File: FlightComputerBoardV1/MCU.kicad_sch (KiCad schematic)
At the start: 22 parts, among them U20 STM32H723ZGTx

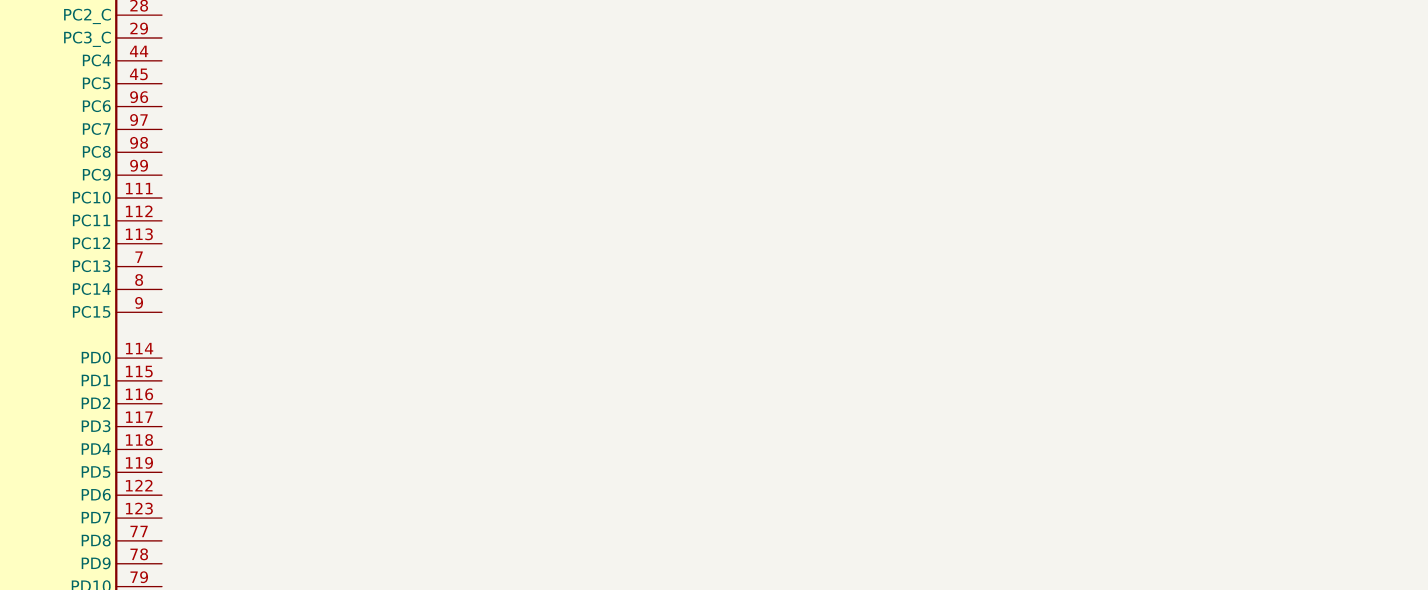
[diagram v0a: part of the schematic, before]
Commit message: Added external clk for mcu sheet
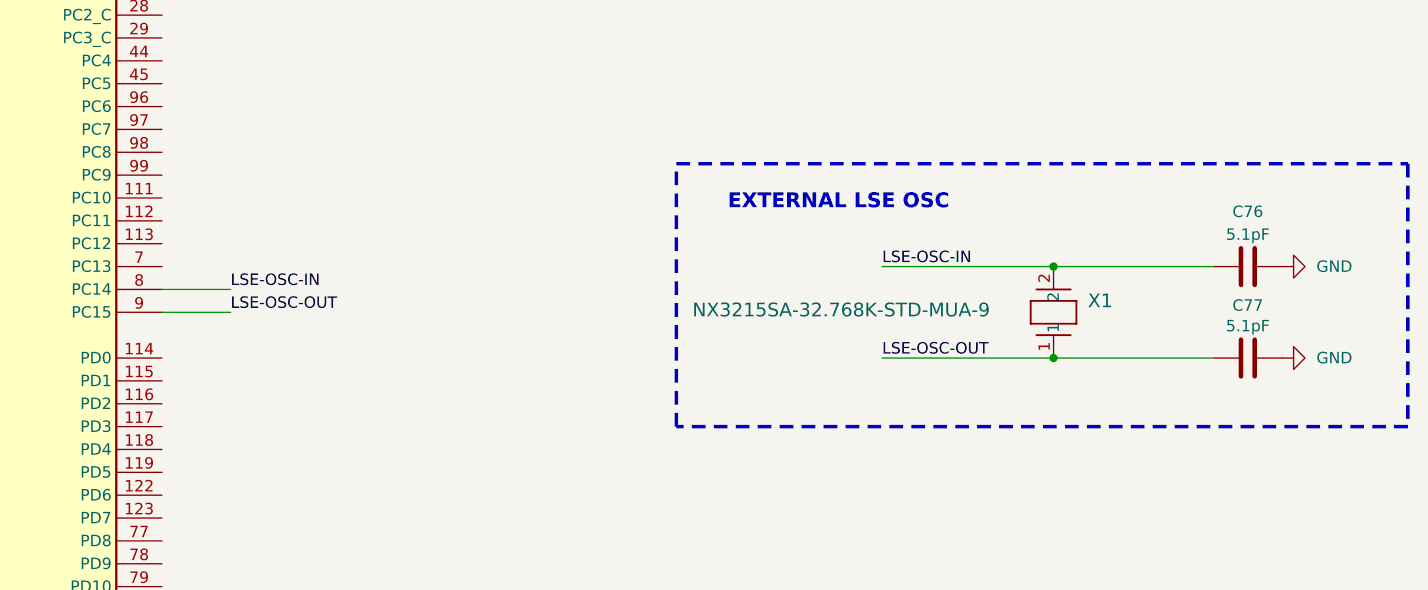
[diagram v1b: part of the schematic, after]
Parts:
- added C76, C77: 5.1pF, XTAL_NX3215SA_NDK, symbol Device:C
- added X1: NX3215SA-32.768K-STD-MUA-9, XTAL_NX3215SA_NDK, symbol LSE-OSC:NX3215SA-32.768K-STD-MUA-9
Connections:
- net GND: now also C76.2, C77.1
- net LSE-OSC-IN: now reaches U20.8 (PC14)
- net LSE-OSC-IN: now also C76.1, X1.2
- net LSE-OSC-OUT: now reaches U20.9 (PC15)
- net LSE-OSC-OUT: now also C77.2, X1.1
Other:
- note added: "EXTERNAL LSE OSC"

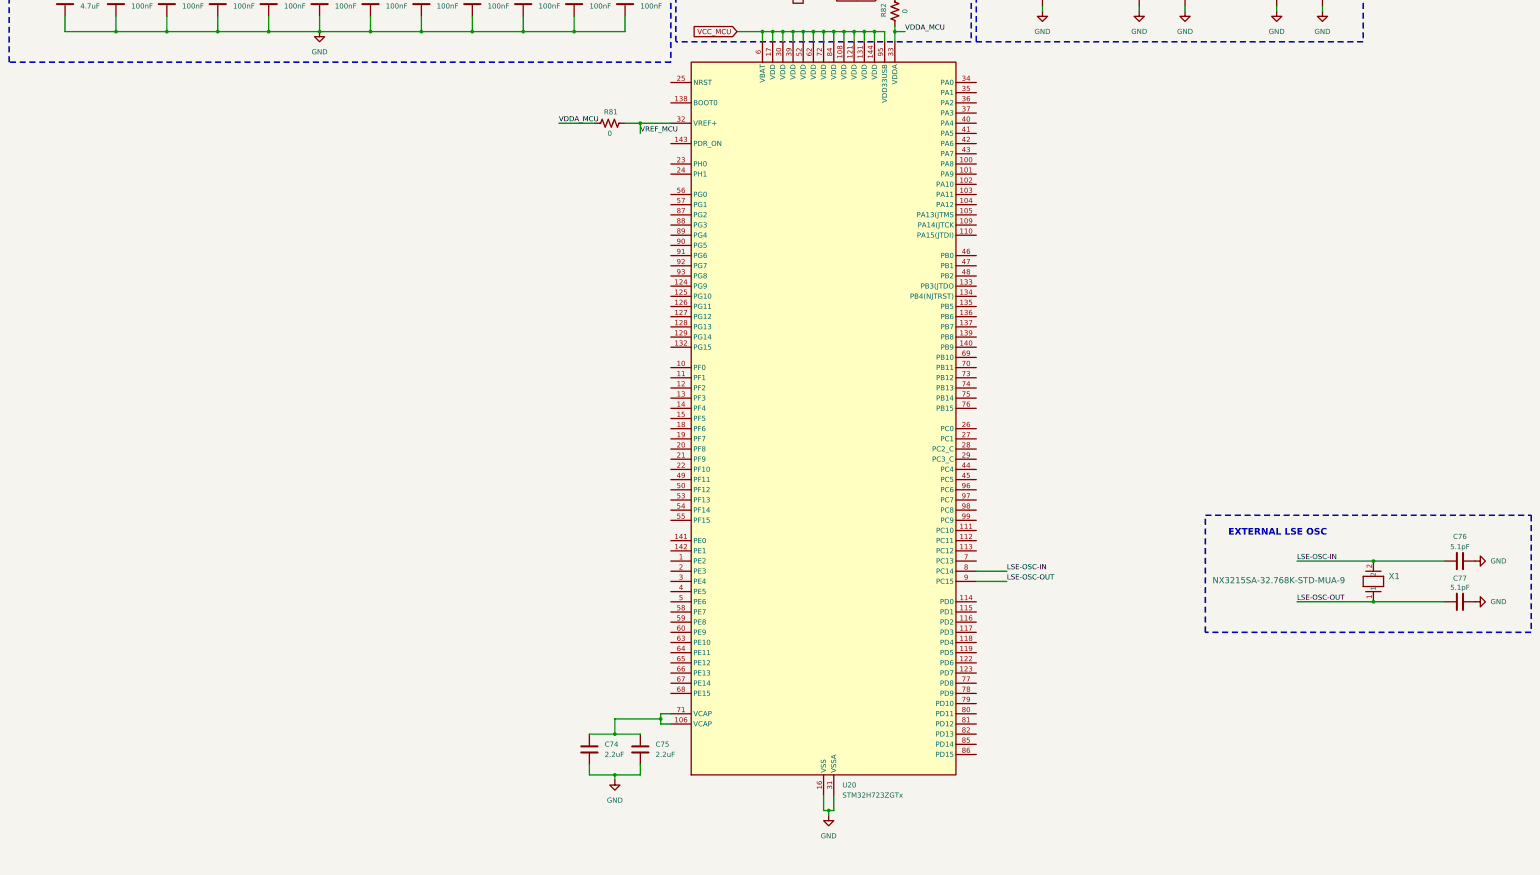
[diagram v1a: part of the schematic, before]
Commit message: Addition to MCU sheet and peripheral connection complete
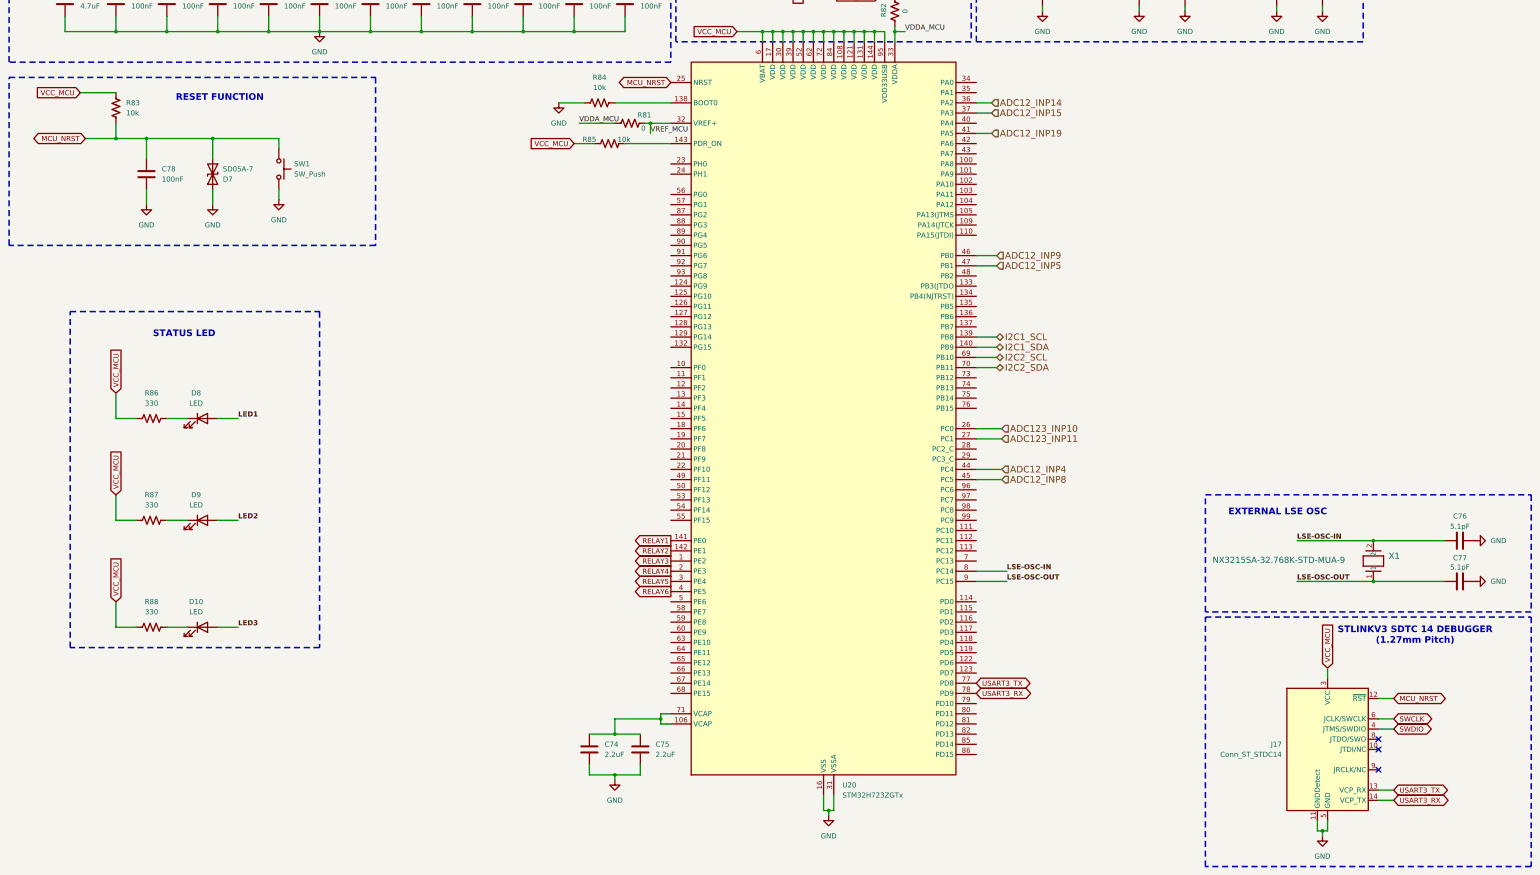
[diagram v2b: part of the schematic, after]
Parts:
- added C78: 100nF, symbol Device:C
- added D10, D8, D9: LED, symbol Device:LED
- added D7: SD05A-7, Diode_SMD:D_SOD-323_HandSoldering, symbol Diode:SD05C-01F
- added J17: Conn_ST_STDC14, Connector_PinHeader_1.27mm:PinHeader_2x07_P1.27mm_Vertical, symbol Connector:Conn_ST_STDC14
- added R83, R84, R85: 10k, Resistor_THT:R_Array_SIP4, symbol Device:R_US
- added R86, R87, R88: 330, Resistor_THT:R_Array_SIP4, symbol Device:R_US
- added SW1: SW_Push, Button_Switch_THT:SW_PUSH_6mm_H4.3mm, symbol Switch:SW_Push
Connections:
- net +3V3: now also J17.3 (VCC), R83.1, R85.1, R86.1, R87.1, R88.1
- net GND: now also C78.2, D7.2 (A2), J17.11 (GNDDetect), J17.5 (GND), J17.7 (GND), R84.1, SW1.2
- net RELAY3: now reaches U20.1 (PE2)
- net at U20.138 (BOOT0): now also R84.2
- net I2C1_SCL: now reaches U20.139 (PB8)
- net I2C1_SDA: now reaches U20.140 (PB9)
- net RELAY1: now reaches U20.141 (PE0)
- net RELAY2: now reaches U20.142 (PE1)
- net at U20.143 (PDR_ON): now also R85.2
- net RELAY4: now reaches U20.2 (PE3)
- net MCU_NRST: now reaches U20.25 (NRST)
- net MCU_NRST: now also C78.1, D7.1 (A1), J17.12 (~{RST}), R83.2, SW1.1
- net ADC123_INP10: now reaches U20.26 (PC0)
- net ADC123_INP11: now reaches U20.27 (PC1)
- net RELAY5: now reaches U20.3 (PE4)
- net ADC12_INP14: now reaches U20.36 (PA2)
- net ADC12_INP15: now reaches U20.37 (PA3)
- net RELAY6: now reaches U20.4 (PE5)
- net ADC12_INP19: now reaches U20.41 (PA5)
- net ADC12_INP4: now reaches U20.44 (PC4)
- net ADC12_INP8: now reaches U20.45 (PC5)
- net ADC12_INP9: now reaches U20.46 (PB0)
- net ADC12_INP5: now reaches U20.47 (PB1)
- net I2C2_SCL: now reaches U20.69 (PB10)
- net I2C2_SDA: now reaches U20.70 (PB11)
- net USART3_TX: now reaches U20.77 (PD8)
- net USART3_TX: now also J17.13 (VCP_RX)
- net USART3_RX: now reaches U20.78 (PD9)
- net USART3_RX: now also J17.14 (VCP_TX)
- new net: D9.1 (K), R87.2
- new net: D8.1 (K), R86.2
- new net: D10.1 (K), R88.2
- new net LED1: D8.2 (A)
- new net LED2: D9.2 (A)
- new net LED3: D10.2 (A)
- new net SWCLK: J17.6 (JCLK/SWCLK)
- new net SWDIO: J17.4 (JTMS/SWDIO)
- no-connect marks 0 -> 3
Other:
- note added: "RESET FUNCTION"
- note added: "STATUS LED"
- note added: "STLINKV3 SDTC 14 DEBUGGER (1.27mm Pitch)"
- moved on the sheet: C76, C77, R81, X1

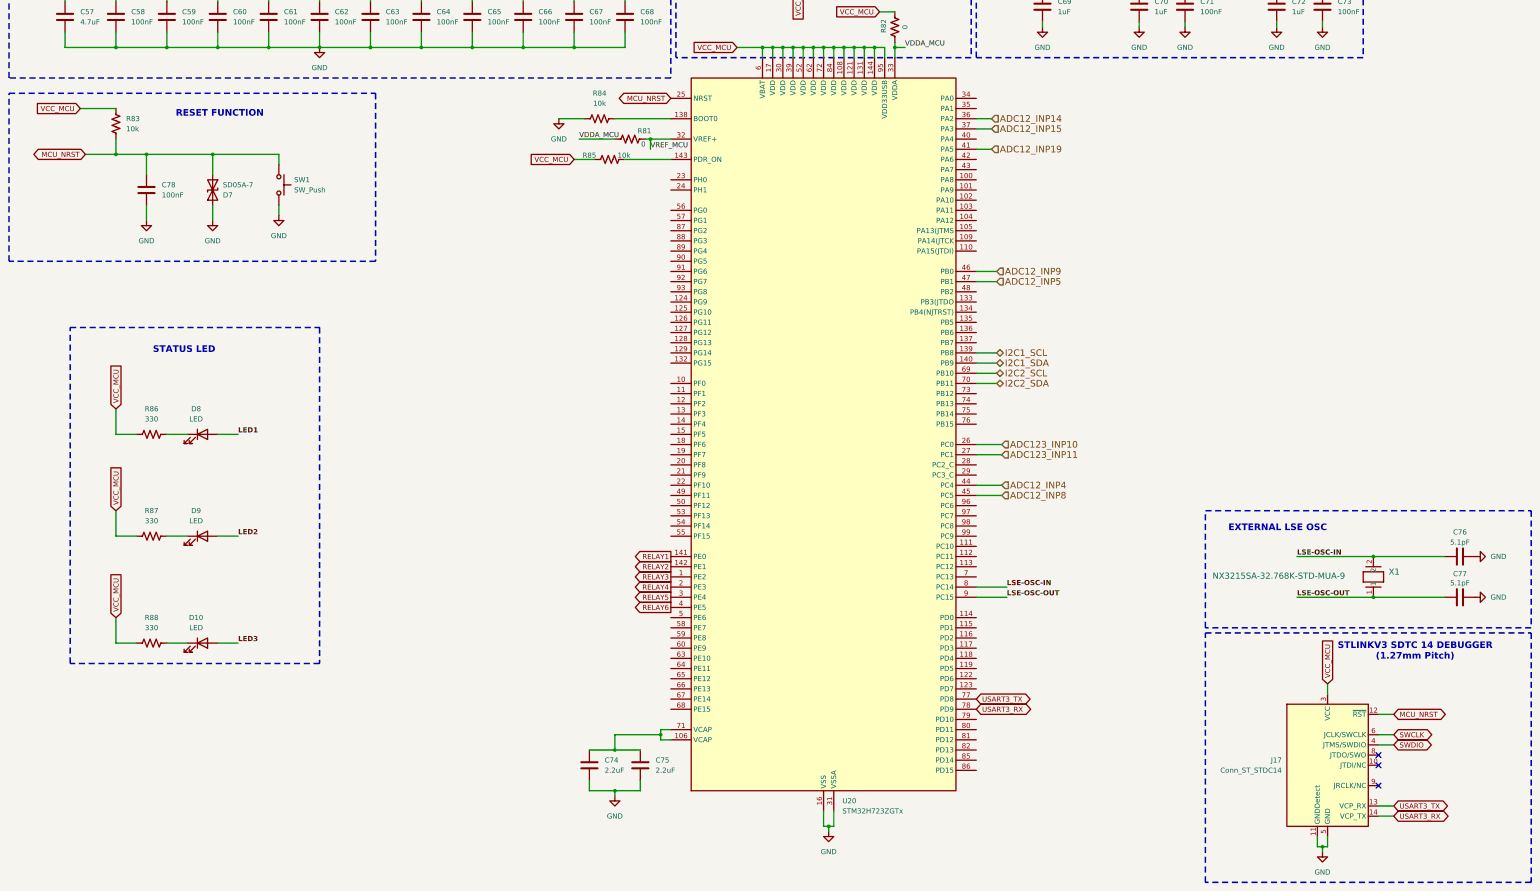
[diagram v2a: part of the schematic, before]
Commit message: added usb-c and boot mode circuit
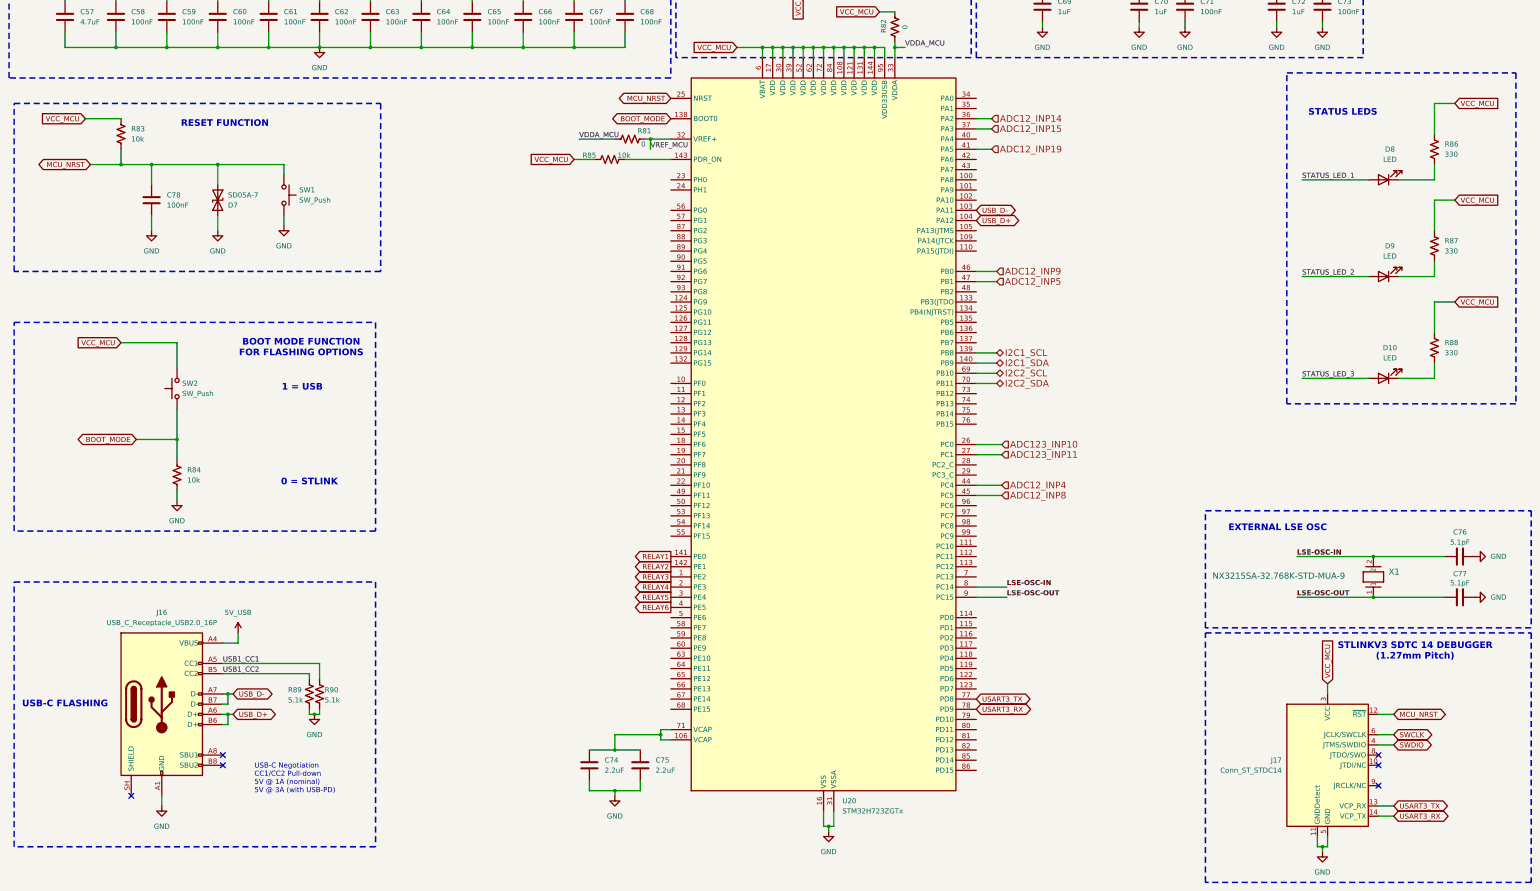
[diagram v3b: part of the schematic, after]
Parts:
- added J16: USB_C_Receptacle_USB2.0_16P, Package_DFN_QFN:WDFN-10-1EP_3x3mm_P0.5mm_EP1.8x2.5mm, symbol Connector:USB_C_Receptacle_USB2.0_16P
- added R89, R90: 5.1k, Resistor_THT:R_Array_SIP4, symbol Device:R_US
- added SW2: SW_Push, Button_Switch_THT:SW_PUSH_6mm_H4.3mm, symbol Switch:SW_Push
- R84: footprint Resistor_THT:R_Array_SIP4 -> (none)
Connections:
- net +3V3: now also SW2.2
- net GND: now also R84.2, J16.A1 (GND), J16.A12 (GND), J16.B1 (GND), J16.B12 (GND), R89.2, R90.2; no longer R84.1
- net BOOT_MODE: now reaches U20.138 (BOOT0)
- net BOOT_MODE: now also R84.1, SW2.1; no longer R84.2
- net USB_D-: now reaches U20.103 (PA11)
- net USB_D-: now also J16.A7 (D-), J16.B7 (D-)
- net USB_D+: now reaches U20.104 (PA12)
- net USB_D+: now also J16.A6 (D+), J16.B6 (D+)
- net LED1 renamed STATUS_LED_1
- net LED2 renamed STATUS_LED_2
- net LED3 renamed STATUS_LED_3
- new net 5V_USB: J16.A4 (VBUS), J16.A9 (VBUS), J16.B4 (VBUS), J16.B9 (VBUS)
- new net USB1_CC1: J16.A5 (CC1), R90.1
- new net USB1_CC2: J16.B5 (CC2), R89.1
- no-connect marks 3 -> 6
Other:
- note added: "0 = STLINK"
- note added: "1 = USB"
- note added: "BOOT MODE FUNCTION FOR FLASHING OPTIONS"
- note added: "STATUS LEDS"
- note added: "USB-C FLASHING"
- note added: "USB-C Negotiation CC1/CC2 Pull-down 5V @ 1A (nominal) 5V @ 3A (with USB-PD)"
- note removed: "STATUS LED"
- moved on the sheet: C78, D7, R83, SW1
